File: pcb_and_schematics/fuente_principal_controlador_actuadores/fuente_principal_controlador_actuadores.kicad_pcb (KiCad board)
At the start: 2 copper layers, 74 parts, among them J1 Screw_Terminal_01x02, J10 Screw_Terminal_01x02, J11 Conn_01x15_Female, J12 Conn_01x15_Female, J2 Screw_Terminal_01x02, J3 Screw_Terminal_01x02, J4 Screw_Terminal_01x02, J5 Screw_Terminal_01x02, J6 Screw_Terminal_01x02, J7 Screw_Terminal_01x02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

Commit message: pcb layout organized and ready for autorouting
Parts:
- Rpullup1, Rpullup2, Rpullup3, Rpullup4, Rpullup5, Rpullup6, Rpullup7, Rpullup8, Rtransistor1, Rtransistor2, Rtransistor3, Rtransistor4, Rtransistor5, Rtransistor6, Rtransistor7, Rtransistor8: footprint Resistor_THT:R_Axial_DIN0207_L6.3mm_D2.5mm_P7.62mm_Horizontal -> Resistor_THT:R_Axial_DIN0207_L6.3mm_D2.5mm_P2.54mm_Vertical
- moved Rsensor2 173.9 mm to (55.3, 130.0)
- moved Rsensor1 172.4 mm to (30.5, 128.7)
- moved J2 161.6 mm to (23.6, 82.7), turned to 90 degrees
- moved C5 148.5 mm to (60.5, 83.0)
- moved C4 146.3 mm to (35.1, 82.3)
- moved J1 145.0 mm to (24.3, 36.0), turned to 90 degrees
- moved Rpullup8 138.5 mm to (241.9, 107.3), turned to 180 degrees
- moved Q8 132.9 mm to (253.4, 115.9), turned to -90 degrees
- moved C3 131.8 mm to (60.5, 56.3)
- moved C1 130.0 mm to (35.1, 36.0)
- moved R1 121.7 mm to (70.6, 33.5)
- moved Rtransistor8 121.5 mm to (253.4, 104.9), turned to -90 degrees
- moved Opto8 118.4 mm to (238.0, 114.7)
- moved U1 116.6 mm to (45.2, 33.5)
- moved C2 115.7 mm to (60.5, 36.0)
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
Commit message: pre autorouting check backup
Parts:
- added Hole1: MountingHole_2.5mm, MountingHole:MountingHole_2.5mm, F.Cu at (31.0, 25.7)
- added Hole2: MountingHole_2.5mm, MountingHole:MountingHole_2.5mm, F.Cu at (269.5, 24.4)
- added Hole3: MountingHole_2.5mm, MountingHole:MountingHole_2.5mm, F.Cu at (265.6, 150.6)
- added Hole4: MountingHole_2.5mm, MountingHole:MountingHole_2.5mm, F.Cu at (28.7, 147.7)
- moved Rtransistor1 9.27 mm to (174.3, 45.7)
- moved Rtransistor5 8.73 mm to (262.4, 64.7)
- moved Rtransistor8 8.73 mm to (261.9, 106.9)
- moved C1 8.73 mm to (43.6, 38.0)
- moved C2 8.73 mm to (69.0, 38.0)
- moved C3 8.73 mm to (69.0, 58.3)
- moved C4 8.73 mm to (43.6, 84.3)
- moved C5 8.73 mm to (69.0, 85.0)
- moved D1 8.73 mm to (81.7, 42.5)
- moved D2 8.73 mm to (81.7, 63.1)
- moved D3 8.73 mm to (82.3, 90.1)
- moved J10 8.73 mm to (229.4, 144.6)
- moved J11 8.73 mm to (129.1, 70.0)
- moved J12 8.73 mm to (103.4, 70.0)
- moved J2 8.73 mm to (32.1, 84.7)
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
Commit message: resizing of pads that involve high currents
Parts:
- moved Hole2 81.5 mm to (188.0, 23.6)
- moved Hole4 47.5 mm to (23.4, 100.5)
- moved J11 39.9 mm to (90.1, 61.5)
- moved Hole3 38.2 mm to (238.2, 124.0)
- moved Opto2 28.1 mm to (220.0, 21.9)
- moved Q2 28.1 mm to (237.1, 28.3)
- moved R_actuator2 28.1 mm to (209.2, 21.9)
- moved Rpullup2 28.1 mm to (223.9, 34.0)
- moved Rtransistor2 28.1 mm to (237.1, 35.2)
- moved Rtransistor5 28.0 mm to (235.8, 55.9)
- moved R_actuator5 28.0 mm to (208.6, 64.5)
- moved Rpullup5 28.0 mm to (224.0, 58.7)
- moved Q5 28.0 mm to (235.6, 65.7)
- moved Opto5 28.0 mm to (220.1, 64.5)
- moved Hole1 27.0 mm to (23.8, 51.7)
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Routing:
- net Net-(C1-Pad1): track 0.00 -> 0.85 mm

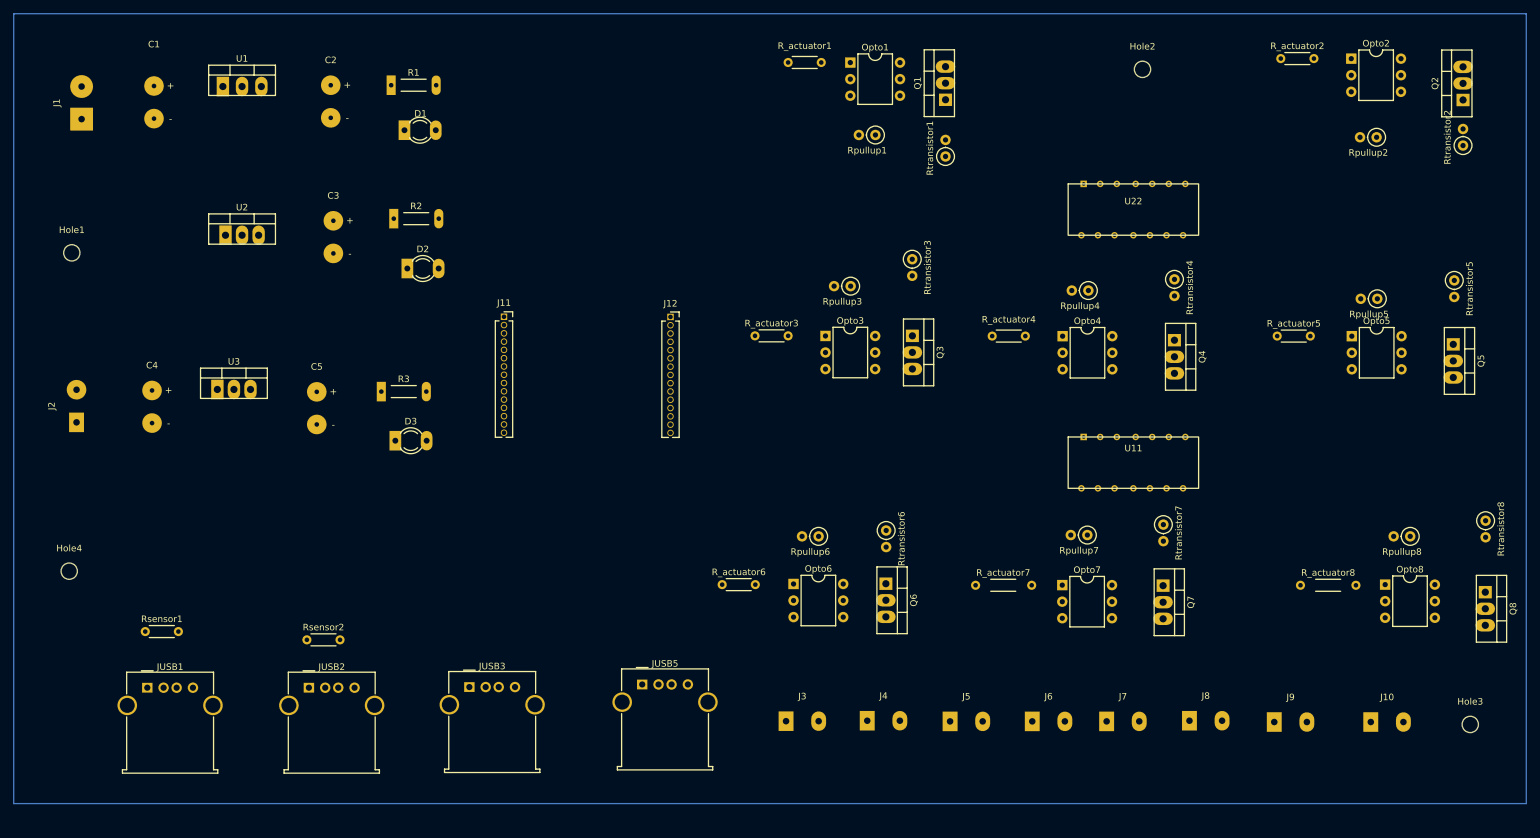
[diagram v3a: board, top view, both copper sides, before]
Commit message: addition of net classes, and changes in footprint of resistors
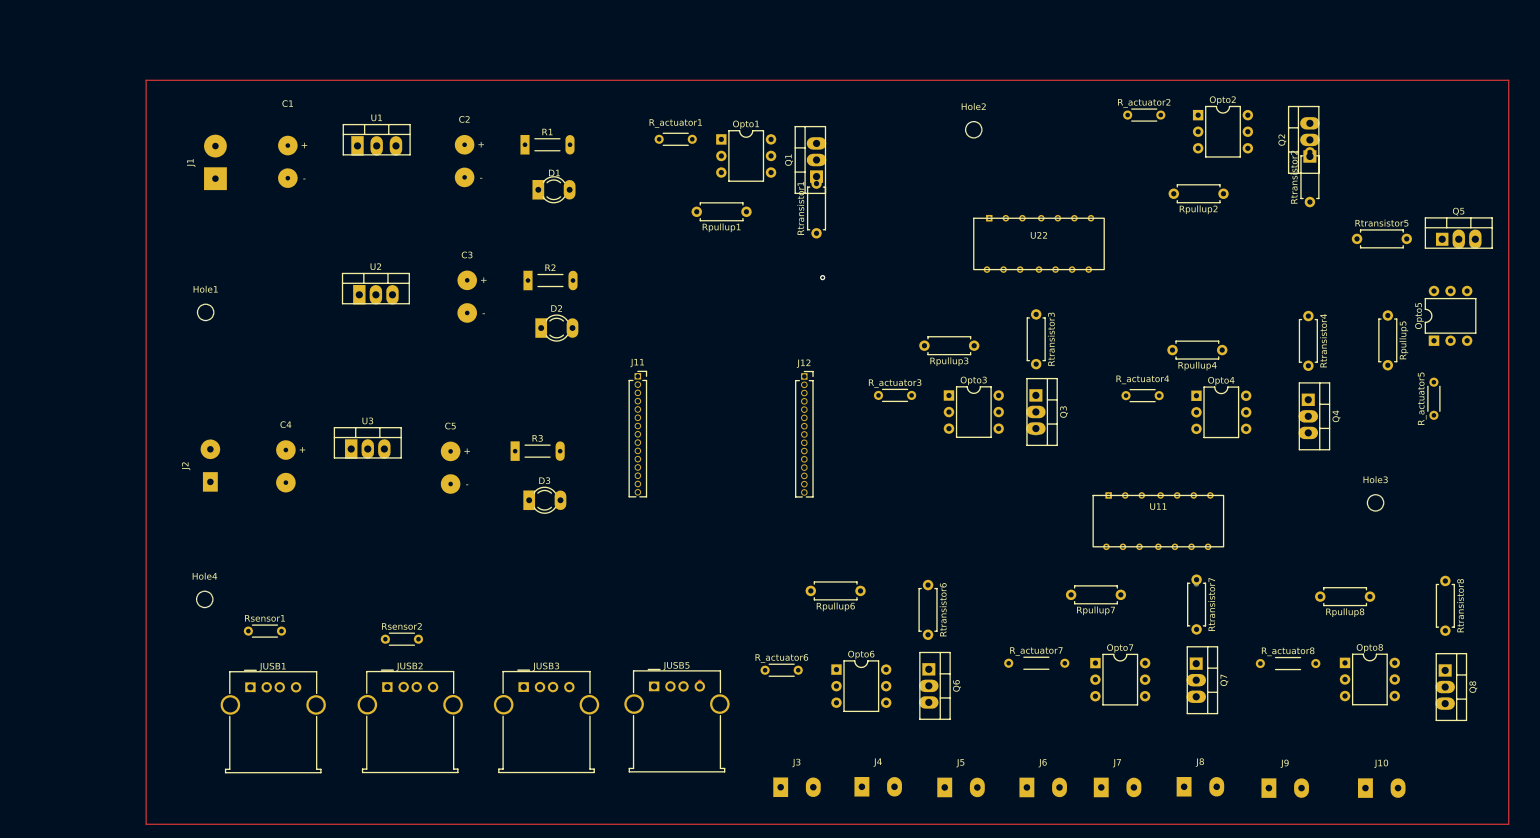
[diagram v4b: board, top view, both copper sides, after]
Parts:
- Rpullup1, Rpullup2, Rpullup3, Rpullup4, Rpullup5, Rpullup6, Rpullup7, Rpullup8, Rtransistor1, Rtransistor2, Rtransistor3, Rtransistor4, Rtransistor5, Rtransistor6, Rtransistor7, Rtransistor8: footprint Resistor_THT:R_Axial_DIN0207_L6.3mm_D2.5mm_P2.54mm_Vertical -> Resistor_THT:R_Axial_DIN0207_L6.3mm_D2.5mm_P7.62mm_Horizontal
- moved Hole3 36.9 mm to (223.7, 90.0)
- moved Hole2 27.5 mm to (162.1, 32.8)
- moved R_actuator5 26.9 mm to (232.7, 76.6), turned to 90 degrees
- moved Opto2 25.0 mm to (196.5, 30.6)
- moved Q2 25.0 mm to (213.7, 36.9)
- moved R_actuator2 25.0 mm to (185.7, 30.6)
- moved Rpullup2 25.0 mm to (200.4, 42.6)
- moved Rtransistor2 25.0 mm to (213.7, 43.9)
- moved Rtransistor1 23.0 mm to (138.0, 48.7)
- moved Q1 23.0 mm to (138.0, 40.0)
- moved Opto1 23.0 mm to (123.4, 34.3)
- moved R_actuator1 23.0 mm to (113.9, 34.3)
- moved Rpullup1 23.0 mm to (127.3, 45.4)
- moved R2 22.7 mm to (94.7, 55.9)
- moved U1 22.6 mm to (68.0, 35.3)
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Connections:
- net 12.0VDC renamed 12.0VDC pot
- net 5.0VDC renamed 5.0VDC pot
- net GND potencia renamed GND pot
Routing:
- net GND 3.3V: track 0.00 -> 1.00 mm
- net Net-(C1-Pad1): track 0.85 -> 0.23 mm
- net pump1: vias 0 -> 1

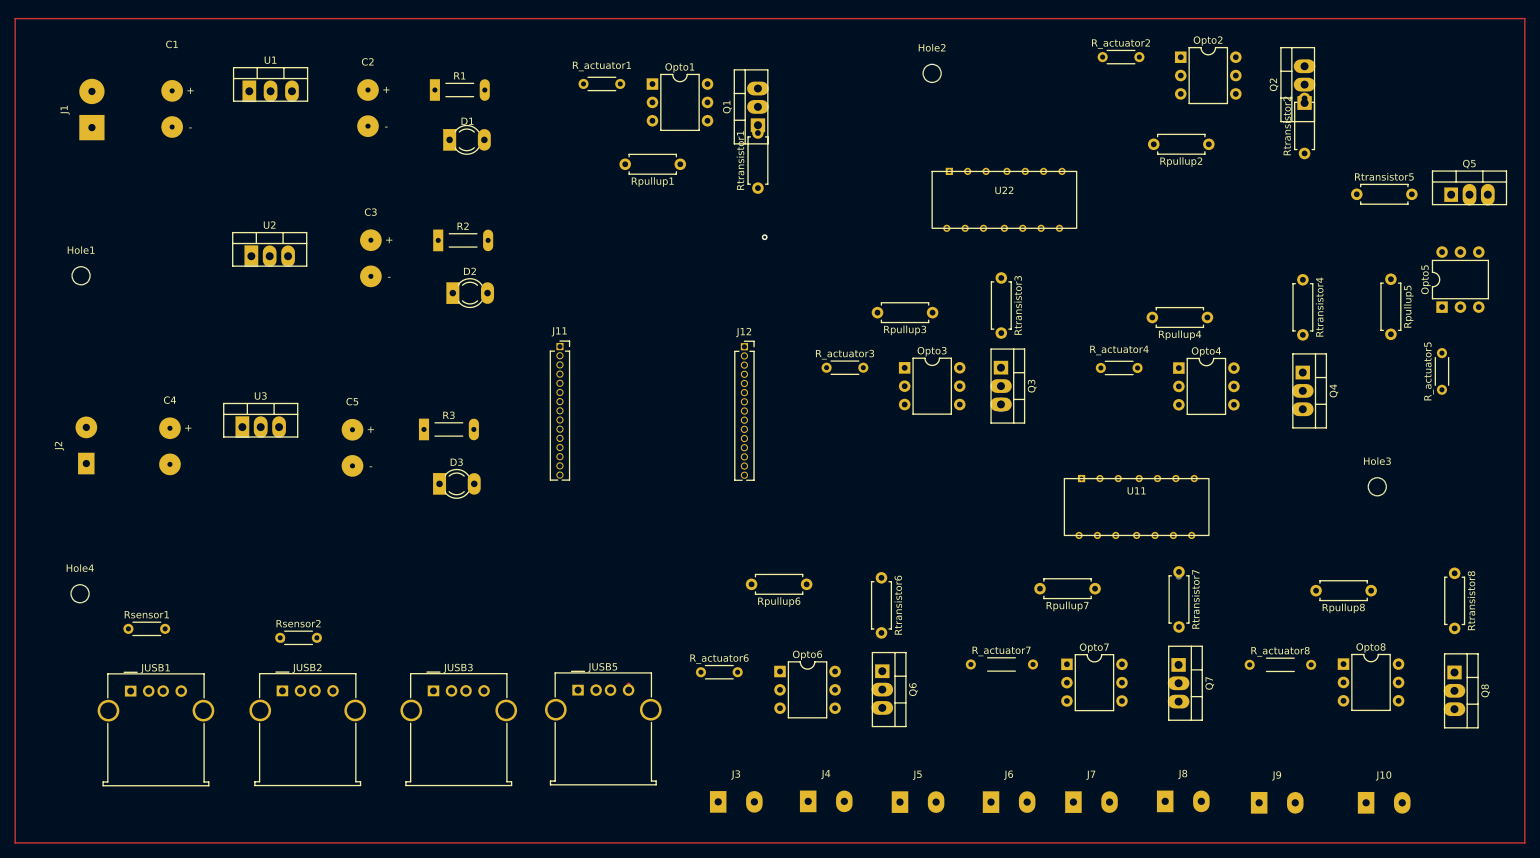
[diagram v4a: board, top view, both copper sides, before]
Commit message: reestructuration of the entire pcb for decreasing the occupied space
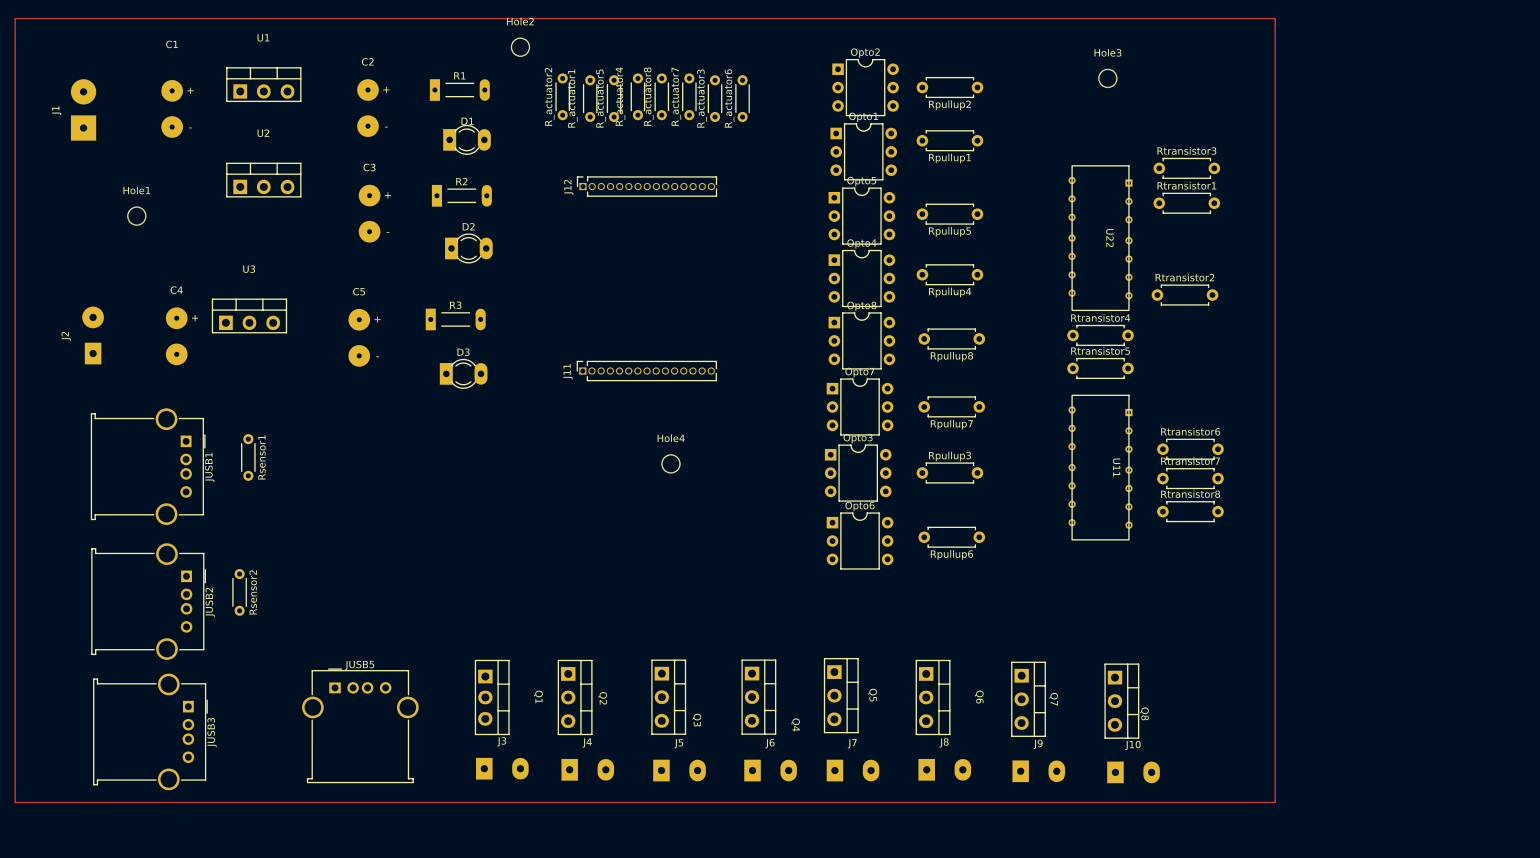
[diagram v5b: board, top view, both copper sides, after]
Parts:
- Q1, Q2, Q3, Q4, Q5, Q6, Q7, Q8, U1, U2, U3: footprint Package_TO_SOT_THT:TO-220-3_Vertical -> maticas:tip122_more_clearence
- moved Q2 130.3 mm to (112.6, 119.1), turned to -90 degrees
- moved R_actuator5 120.6 mm to (118.1, 38.9)
- moved R_actuator8 112.6 mm to (124.7, 38.6), turned to 90 degrees
- moved Q5 109.3 mm to (149.4, 118.9), turned to -90 degrees
- moved Q4 87.8 mm to (138.0, 119.1)
- moved Q1 87.3 mm to (101.1, 119.1), turned to -90 degrees
- moved R_actuator7 86.2 mm to (128.5, 38.6), turned to 90 degrees
- moved Opto5 85.4 mm to (148.6, 50.0), turned to 0 degrees
- moved Opto8 84.8 mm to (148.6, 67.3)
- moved Hole4 83.7 mm to (126.0, 86.9)
- moved R_actuator6 77.0 mm to (135.9, 38.9), turned to 90 degrees
- moved R_actuator2 75.1 mm to (111.0, 38.6), turned to 90 degrees
- moved R_actuator4 73.0 mm to (121.4, 38.6), turned to 90 degrees
- moved Hole3 67.7 mm to (186.4, 33.5)
- moved Q3 64.8 mm to (125.5, 119.1)
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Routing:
- net GND 3.3V: track 1.00 -> 0.00 mm
- net pump1: vias 1 -> 0

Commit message: reestructuration of pin connections in the schematic
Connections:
- J11 pad 4: 3.3V ec -> signal PH
- J11 pad 5: GND ec -> signal EC
- J11 pad 6: signal EC -> 3.3V ec
- J11 pad 7: signal PH -> GND ec
- J11 pad 8: unconnected-(J11-Pad8) -> signal DB18B20
- J11 pad 9: unconnected-(J11-Pad9) -> Signal ExtraSensor
- J12 pad 10: signal DB18B20 -> lights
- J12 pad 11: unconnected-(J12-Pad11) -> mainWaterPump
- J12 pad 4: pump2 -> unconnected-(J12-Pad4)
- J12 pad 5: pump3 -> pump2
- J12 pad 6: pump4 -> unconnected-(J12-Pad6)
- J12 pad 7: lights -> unconnected-(J12-Pad7)
- J12 pad 8: mainWaterPump -> pump3
- J12 pad 9: Signal ExtraSensor -> pump4
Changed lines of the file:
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@@
   (net 21 "signal EC")
   (net 22 "signal PH")
-  (net 23 "unconnected-(J11-Pad8)")
-  (net 24 "unconnected-(J11-Pad9)")
+  (net 23 "unconnected-(J12-Pad4)")
+  (net 24 "unconnected-(J12-Pad6)")
   (net 25 "unconnected-(J11-Pad10)")
   (net 26 "unconnected-(J11-Pad11)")
@@
   (net 37 "Signal ExtraSensor")
   (net 38 "signal DB18B20")
-  (net 39 "unconnected-(J12-Pad11)")
+  (net 39 "unconnected-(J12-Pad7)")
   (net 40 "unconnected-(J12-Pad12)")
   (net 41 "unconnected-(J12-Pad13)")
@@
       (net 18 "unconnected-(J11-Pad3)") (pinfunction "Pin_3") (pintype "passive"))
     (pad "4" thru_hole oval (at 0 3.81 90) (size 1 1) (drill 0.7) (layers *.Cu *.Mask)
-      (net 19 "3.3V ec") (pinfunction "Pin_4") (pintype "passive"))
+      (net 22 "signal PH") (pinfunction "Pin_4") (pintype "passive"))
     (pad "5" thru_hole oval (at 0 5.08 90) (size 1 1) (drill 0.7) (layers *.Cu *.Mask)
-      (net 20 "GND ec") (pinfunction "Pin_5") (pintype "passive"))
+      (net 21 "signal EC") (pinfunction "Pin_5") (pintype "passive"))
     (pad "6" thru_hole oval (at 0 6.35 90) (size 1 1) (drill 0.7) (layers *.Cu *.Mask)
-      (net 21 "signal EC") (pinfunction "Pin_6") (pintype "passive"))
+      (net 19 "3.3V ec") (pinfunction "Pin_6") (pintype "passive"))
     (pad "7" thru_hole oval (at 0 7.62 90) (size 1 1) (drill 0.7) (layers *.Cu *.Mask)
-      (net 22 "signal PH") (pinfunction "Pin_7") (pintype "passive"))
+      (net 20 "GND ec") (pinfunction "Pin_7") (pintype "passive"))
     (pad "8" thru_hole oval (at 0 8.89 90) (size 1 1) (drill 0.7) (layers *.Cu *.Mask)
-      (net 23 "unconnected-(J11-Pad8)") (pinfunction "Pin_8") (pintype "passive"))
+      (net 38 "signal DB18B20") (pinfunction "Pin_8") (pintype "passive"))
     (pad "9" thru_hole oval (at 0 10.16 90) (size 1 1) (drill 0.7) (layers *.Cu *.Mask)
-      (net 24 "unconnected-(J11-Pad9)") (pinfunction "Pin_9") (pintype "passive"))
+      (net 37 "Signal ExtraSensor") (pinfunction "Pin_9") (pintype "passive"))
     (pad "10" thru_hole oval (at 0 11.43 90) (size 1 1) (drill 0.7) (layers *.Cu *.Mask)
       (net 25 "unconnected-(J11-Pad10)") (pinfunction "Pin_10") (pintype "passive"))
@@
       (net 31 "pump1") (pinfunction "Pin_3") (pintype "passive"))
     (pad "4" thru_hole oval (at 0 3.81 90) (size 1 1) (drill 0.7) (layers *.Cu *.Mask)
-      (net 32 "pump2") (pinfunction "Pin_4") (pintype "passive"))
+      (net 23 "unconnected-(J12-Pad4)") (pinfunction "Pin_4") (pintype "passive"))
     (pad "5" thru_hole oval (at 0 5.08 90) (size 1 1) (drill 0.7) (layers *.Cu *.Mask)
-      (net 33 "pump3") (pinfunction "Pin_5") (pintype "passive"))
+      (net 32 "pump2") (pinfunction "Pin_5") (pintype "passive"))
     (pad "6" thru_hole oval (at 0 6.35 90) (size 1 1) (drill 0.7) (layers *.Cu *.Mask)
-      (net 34 "pump4") (pinfunction "Pin_6") (pintype "passive"))
+      (net 24 "unconnected-(J12-Pad6)") (pinfunction "Pin_6") (pintype "passive"))
     (pad "7" thru_hole oval (at 0 7.62 90) (size 1 1) (drill 0.7) (layers *.Cu *.Mask)
-      (net 35 "lights") (pinfunction "Pin_7") (pintype "passive"))
+      (net 39 "unconnected-(J12-Pad7)") (pinfunction "Pin_7") (pintype "passive"))
     (pad "8" thru_hole oval (at 0 8.89 90) (size 1 1) (drill 0.7) (layers *.Cu *.Mask)
-      (net 36 "mainWaterPump") (pinfunction "Pin_8") (pintype "passive"))
+      (net 33 "pump3") (pinfunction "Pin_8") (pintype "passive"))
     (pad "9" thru_hole oval (at 0 10.16 90) (size 1 1) (drill 0.7) (layers *.Cu *.Mask)
-      (net 37 "Signal ExtraSensor") (pinfunction "Pin_9") (pintype "passive"))
+      (net 34 "pump4") (pinfunction "Pin_9") (pintype "passive"))
     (pad "10" thru_hole oval (at 0 11.43 90) (size 1 1) (drill 0.7) (layers *.Cu *.Mask)
-      (net 38 "signal DB18B20") (pinfunction "Pin_10") (pintype "passive"))
+      (net 35 "lights") (pinfunction "Pin_10") (pintype "passive"))
     (pad "11" thru_hole oval (at 0 12.7 90) (size 1 1) (drill 0.7) (layers *.Cu *.Mask)
-      (net 39 "unconnected-(J12-Pad11)") (pinfunction "Pin_11") (pintype "passive"))
+      (net 36 "mainWaterPump") (pinfunction "Pin_11") (pintype "passive"))
     (pad "12" thru_hole oval (at 0 13.97 90) (size 1 1) (drill 0.7) (layers *.Cu *.Mask)
       (net 40 "unconnected-(J12-Pad12)") (pinfunction "Pin_12") (pintype "passive"))
